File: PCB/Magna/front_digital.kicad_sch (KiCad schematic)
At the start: 0 parts

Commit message: Add final touched to all schematics
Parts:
- added C1801, C1802, C1803, C1804, C1805, C1806, C1807, C1808, C1809, C1810, C1811, C1812, C1813, C1814, C1815, C1816, C1817: 100n, symbol Device:C_Small
- added R1801, R1802, R1803, R1804, R1805, R1810, R1811, R1812, R1813, R1818, R1819, R1820, R1821, R1826, R1827, R1828, R1832: 10k, symbol Device:R_Small
- added R1806, R1807, R1808, R1809, R1814, R1815, R1816, R1817, R1822, R1823, R1824, R1825, R1829, R1830, R1831, R1833: 1k, symbol Device:R_Small
- added SW1801, SW1802, SW1803, SW1804, SW1805, SW1806, SW1807, SW1808, SW1809, SW1810, SW1811, SW1812, SW1813, SW1814, SW1815, SW1816: ~, symbol Switch:SW_Push
- added U1801: XL9535, Package_SO:TSSOP-24_4.4x7.8mm_P0.65mm, symbol Interface_Expansion:TCA9535PWR
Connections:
- new net: R1809.2, SW1804.1
- new net: R1815.2, SW1806.1
- new net: R1830.2, SW1814.1
- new net: R1825.2, SW1812.1
- new net: R1829.2, SW1813.1
- new net: R1822.2, SW1809.1
- new net: R1824.2, SW1811.1
- new net: R1806.2, SW1801.1
- new net: R1807.2, SW1802.1
- new net: R1817.2, SW1808.1
- new net: R1814.2, SW1805.1
- new net: R1816.2, SW1807.1
- new net: R1833.2, SW1816.1
- new net: R1831.2, SW1815.1
- new net: R1808.2, SW1803.1
- new net: R1823.2, SW1810.1
- new net COLOUR_SEL_1: C1804.1, R1804.2, R1808.1, U1801.13 (P10)
- new net COLOUR_SEL_2: C1808.1, R1812.2, R1816.1, U1801.14 (P11)
- new net COLOUR_SEL_3: C1812.1, R1820.2, R1824.1, U1801.15 (P12)
- new net COLOUR_SEL_4: C1816.1, R1828.2, R1831.1, U1801.16 (P13)
- new net CUE_CH1_SEL: C1802.1, R1802.2, R1806.1, U1801.4 (P00)
- new net CUE_CH2_SEL: C1806.1, R1810.2, R1814.1, U1801.5 (P01)
- new net CUE_EFFECT_SEL: C1810.1, R1818.2, R1822.1, U1801.6 (P02)
- new net EFFECT ON: C1803.1, R1803.2, R1807.1, U1801.8 (P04)
- new net EFFECT_ASSIGN_CH1: C1807.1, R1811.2, R1815.1, U1801.9 (P05)
- new net EFFECT_ASSIGN_CH2: C1811.1, R1819.2, R1823.1, U1801.10 (P06)
- new net GND: C1801.2, C1802.2, C1803.2, C1804.2, C1805.2, C1806.2, C1807.2, C1808.2, C1809.2, C1810.2, C1811.2, C1812.2, C1813.2, C1814.2, C1815.2, C1816.2, C1817.2, SW1801.2, SW1802.2, SW1803.2, SW1804.2, SW1805.2, SW1806.2, SW1807.2, SW1808.2, SW1809.2, SW1810.2, SW1811.2, SW1812.2, SW1813.2, SW1814.2, SW1815.2, SW1816.2, U1801.12 (GND), U1801.2 (A1), U1801.21 (A0), U1801.3 (A2)
- new net I2C_SCL: U1801.22 (SCL)
- new net I2C_SDA: U1801.23 (SDA)
- new net SPARE_1: C1814.1, R1826.2, R1829.1, U1801.7 (P03)
- new net SPARE_2: C1815.1, R1827.2, R1830.1, U1801.11 (P07)
- new net SPARE_3: C1805.1, R1805.2, R1809.1, U1801.17 (P14)
- new net SPARE_4: C1809.1, R1813.2, R1817.1, U1801.18 (P15)
- new net SPARE_5: C1813.1, R1821.2, R1825.1, U1801.19 (P16)
- new net SPARE_6: C1817.1, R1832.2, R1833.1, U1801.20 (P17)
- new net VDD: C1801.1, R1801.1, R1802.1, R1803.1, R1804.1, R1805.1, R1810.1, R1811.1, R1812.1, R1813.1, R1818.1, R1819.1, R1820.1, R1821.1, R1826.1, R1827.1, R1828.1, R1832.1, U1801.24 (VCC)
- new net button_interrupt: R1801.2, U1801.1 (~{INT})
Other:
- note added: "COLOUR SEL 1"
- note added: "COLOUR SEL 2"
- note added: "COLOUR SEL 3"
- note added: "COLOUR SEL 4"
- note added: "CUE CH1"
- note added: "CUE CH2"
- note added: "CUE EFFECT"
- note added: "EFFECT ASSIGN 1"
- note added: "EFFECT ASSIGN 2"
- note added: "EFFECT ON"
- note added: "SPARE 1"
- note added: "SPARE 2"
- note added: "SPARE 3"
- note added: "SPARE 4"
- note added: "SPARE 5"
- note added: "SPARE 6"

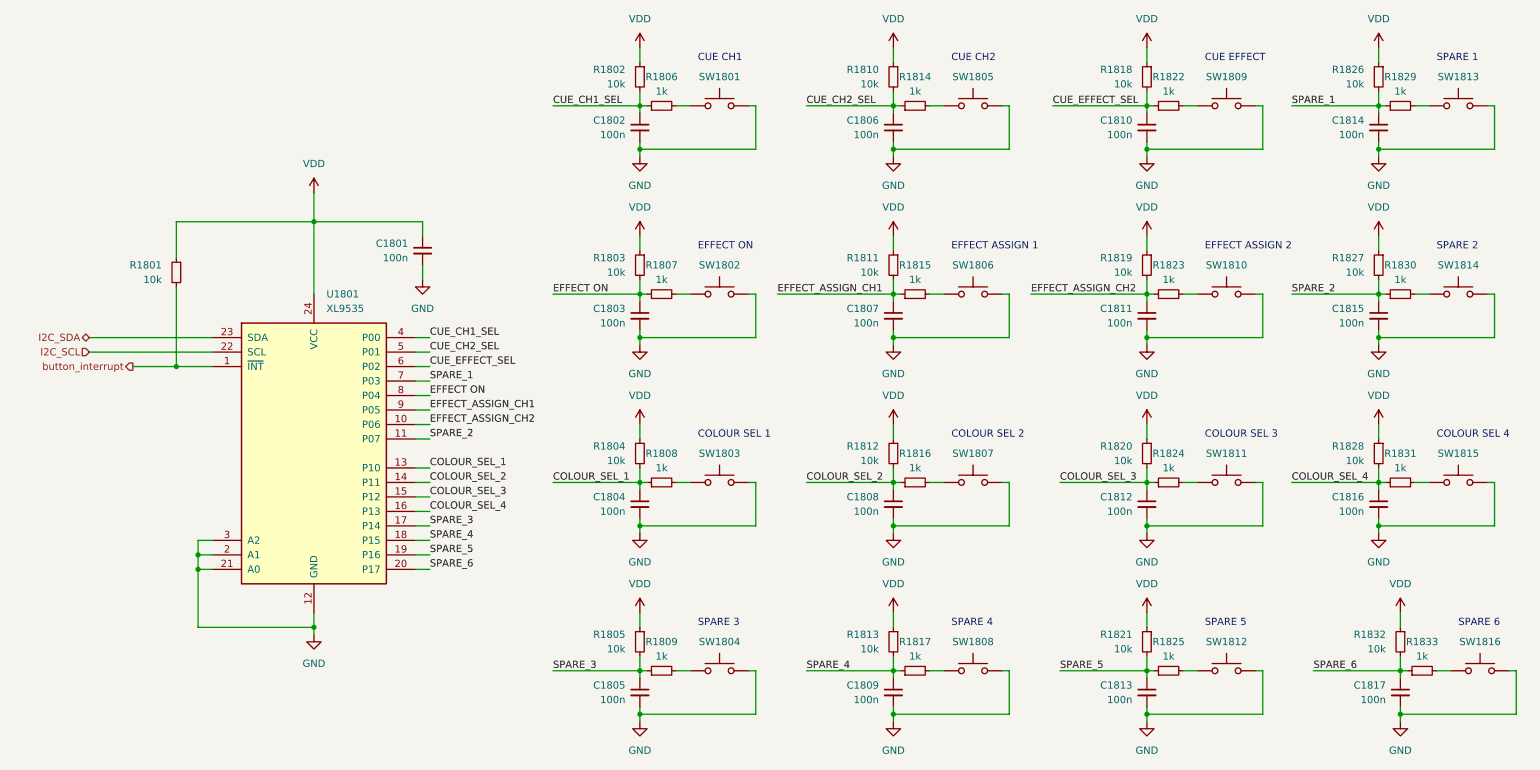
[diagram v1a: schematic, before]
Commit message: Update capacitors to parts in JLC library
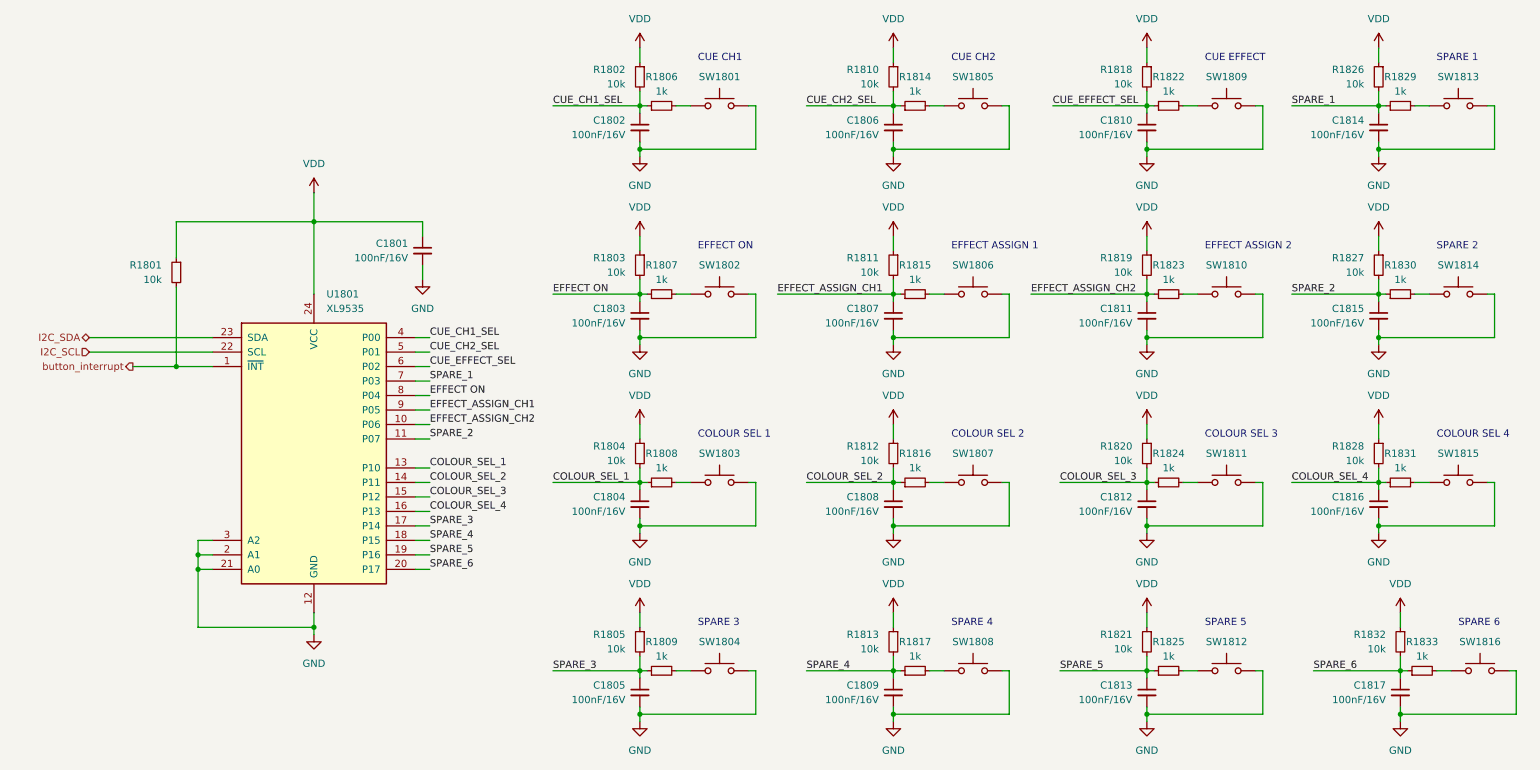
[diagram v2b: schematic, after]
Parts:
- C1801, C1802, C1803, C1804, C1805, C1806, C1807, C1808, C1809, C1810, C1811, C1812, C1813, C1814, C1815, C1816, C1817: value 100n -> 100nF/16V; footprint (none) -> Capacitor_SMD:C_0805_2012Metric; LCSC (none) -> C218638

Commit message: Select parts for all components
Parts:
- R1801, R1802, R1803, R1804, R1805, R1810, R1811, R1812, R1813, R1818, R1819, R1820, R1821, R1826, R1827, R1828, R1832: footprint (none) -> Resistor_SMD:R_0805_2012Metric; LCSC (none) -> C17414
- R1806, R1807, R1808, R1809, R1814, R1815, R1816, R1817, R1822, R1823, R1824, R1825, R1829, R1830, R1831, R1833: footprint (none) -> Resistor_SMD:R_0805_2012Metric_Pad1.20x1.40mm_HandSolder; LCSC (none) -> C17513
- U1801: LCSC (none) -> C561273

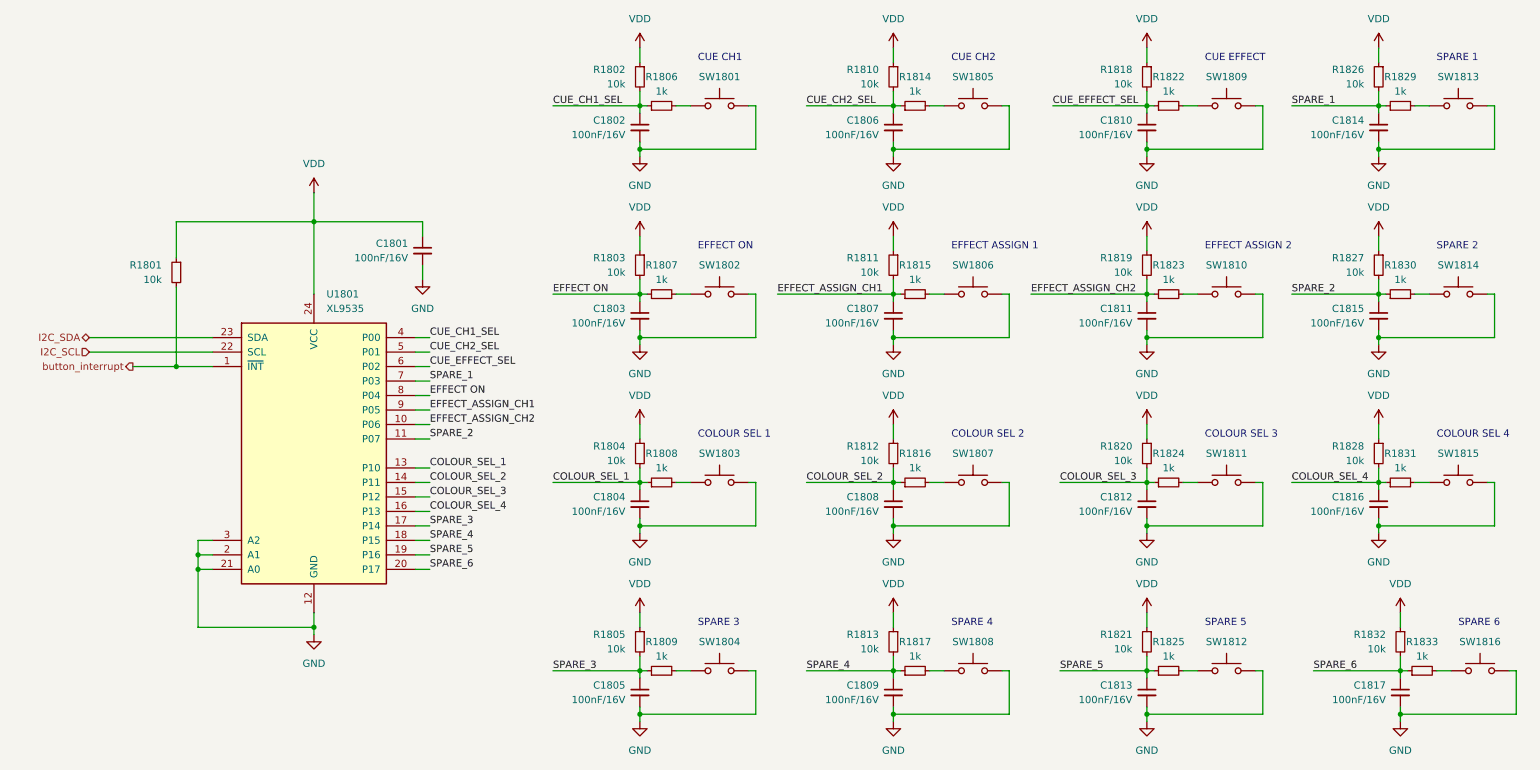
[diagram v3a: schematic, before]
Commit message: Add even more component footprints and partnumbers
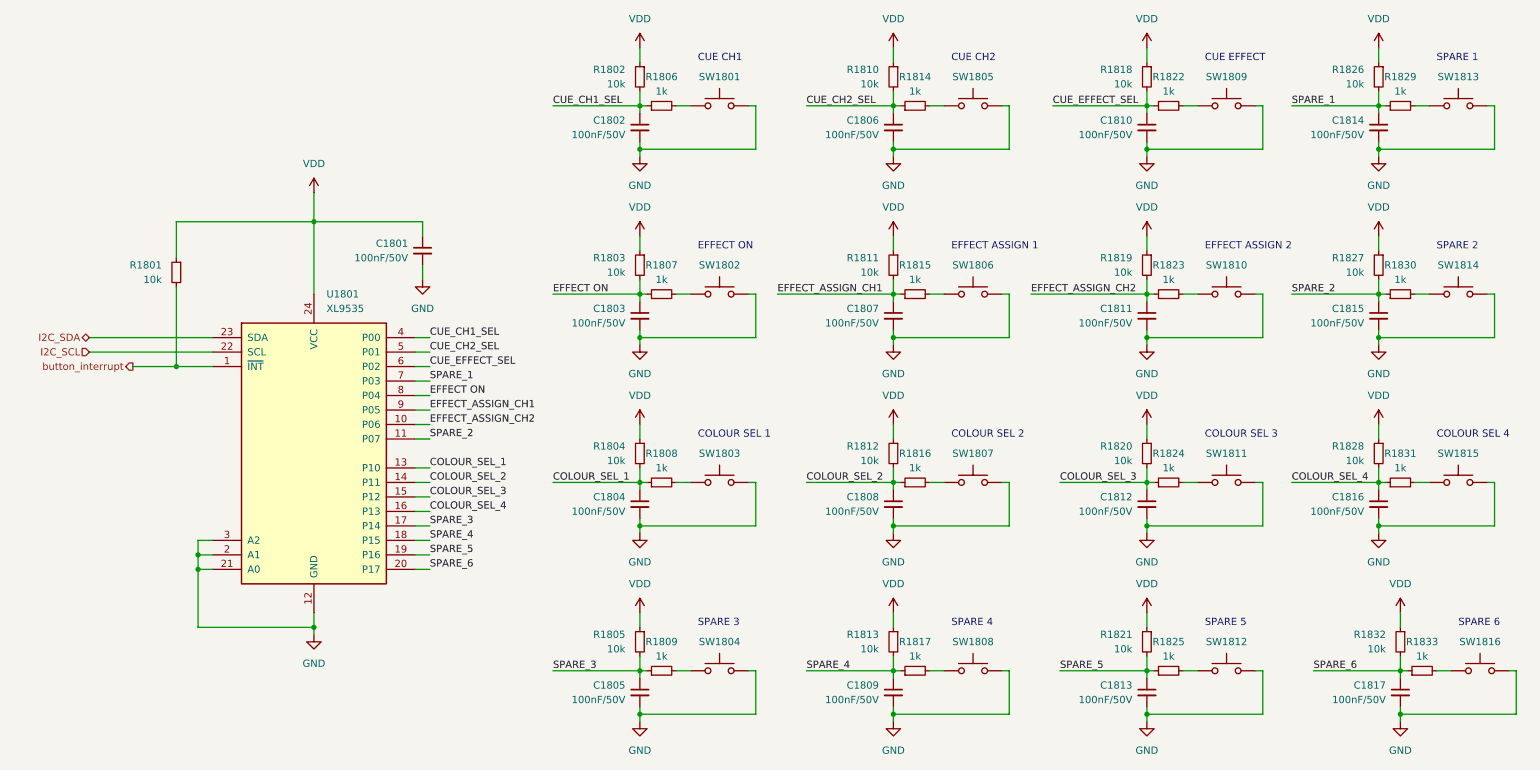
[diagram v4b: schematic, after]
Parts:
- C1801, C1802, C1803, C1804, C1805, C1806, C1807, C1808, C1809, C1810, C1811, C1812, C1813, C1814, C1815, C1816, C1817: value 100nF/16V -> 100nF/50V; footprint Capacitor_SMD:C_0805_2012Metric -> Capacitor_SMD:C_0805_2012Metric_Pad1.18x1.45mm_HandSolder; LCSC C218638 -> C49678
- R1801, R1802, R1803, R1804, R1805, R1810, R1811, R1812, R1813, R1818, R1819, R1820, R1821, R1826, R1827, R1828, R1832: footprint Resistor_SMD:R_0805_2012Metric -> Resistor_SMD:R_0805_2012Metric_Pad1.20x1.40mm_HandSolder
- SW1801, SW1802, SW1803, SW1804, SW1805, SW1806, SW1807, SW1808, SW1809, SW1810, SW1811, SW1812, SW1813, SW1814, SW1815, SW1816: footprint (none) -> Button_Switch_SMD:SW_Push_1P1T_XKB_TS-1187A
